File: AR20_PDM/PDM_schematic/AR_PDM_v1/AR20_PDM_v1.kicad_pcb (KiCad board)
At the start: 2 copper layers, 118 x 112 mm, 253 parts, among them IC1 TMUX1208PWR, J1 S_T_?, J2 1-776163-1, K1 DIPxx-1Cxx-51x, K2 DIPxx-1Cxx-51x, P1 B4B-PH-SM4-TB, Q1 BTS50025-1TAD, Q2 BTS50025-1TAD, Q3 BTS50025-1TAD, Q5 BTS50025-1TAD, Q6 BTS50025-1TAD, Q7 BTS50025-1TAD, Q8 BTS50025-1TAD, SW1 SW_DIP_x07, U1 ACM_2020, U10 N-MOS, U11 N-MOS, U12 P-MOS, U13 N-MOS, U14 N-MOS, U15 NMOS, U16 NMOS, U17 NMOS, U18 NMOS, U19 NMOS, U2 INA233, U20 NMOS, U21 NMOS, U22 NMOS, U23 NMOS, U24 NMOS, U25 NMOS, U26 NMOS, U27 NMOS, U28 NMOS, U29 INA233, U3 INA233, U30 INA233, U31 INA233, U32 Fet-P, U33 Fet-P, U34 Fet-P, U35 Fet-P, U36 Fet-P, U4 INA233, U5 INA233, U6 INA233, U7 INA233, U8 INA233, U9 TCA6424ARGJR

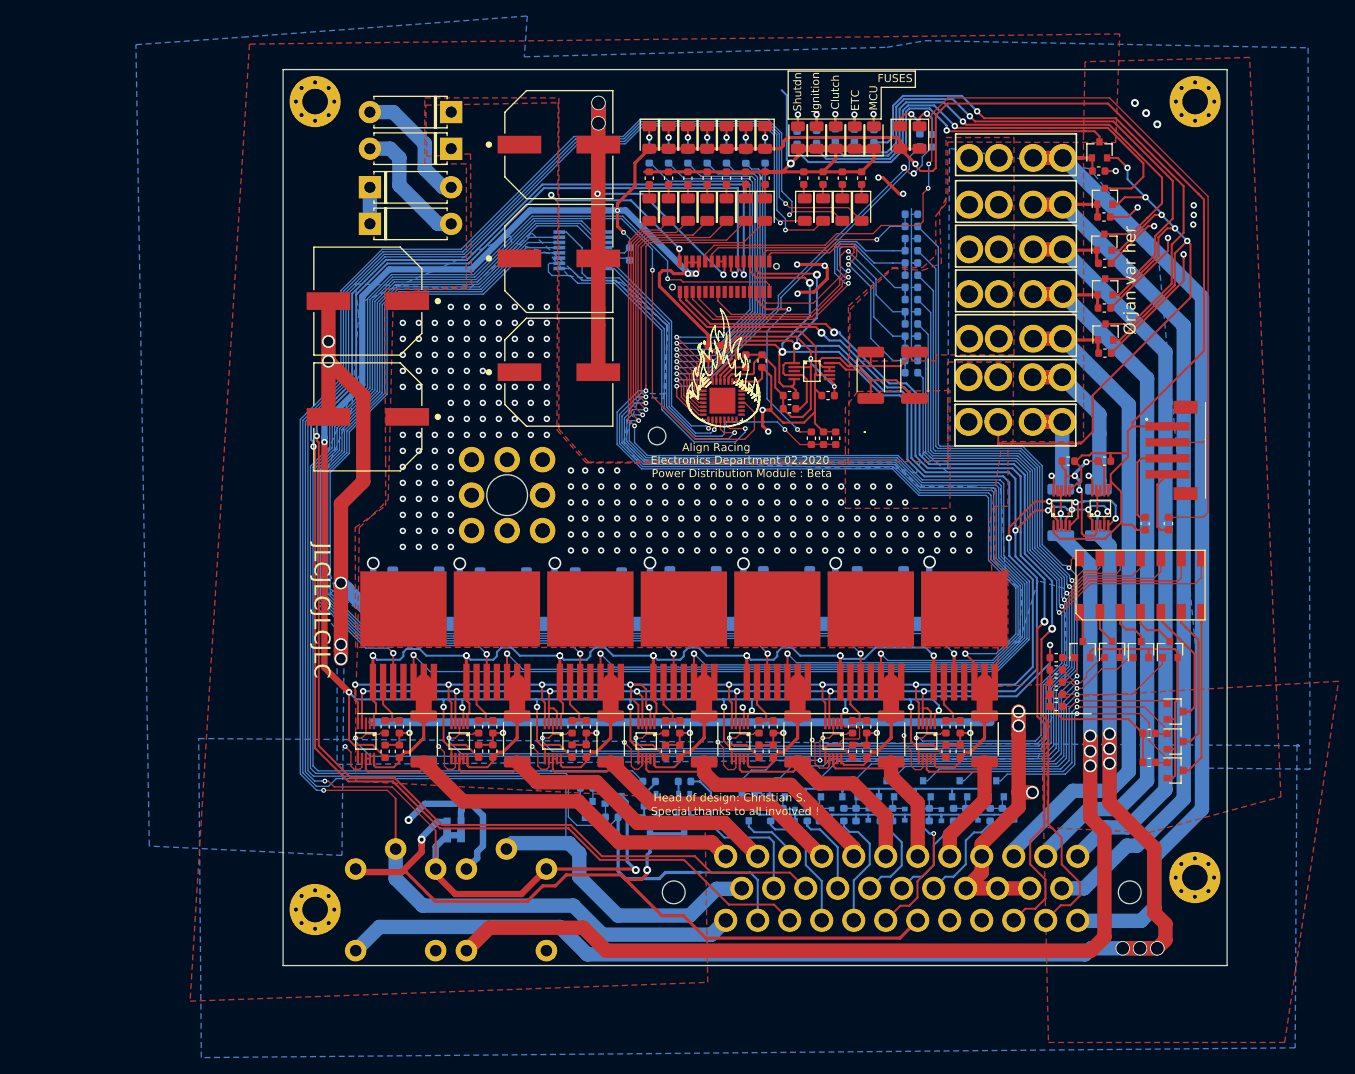
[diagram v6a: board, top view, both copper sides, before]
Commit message: End of Beta beginning of Charlie.
- RE0.2mm rework, jlc pcb minimum clearance with 2 OZ copper, was not advertised, properly
a retrace
Re positioning of some of components
added temp sensor
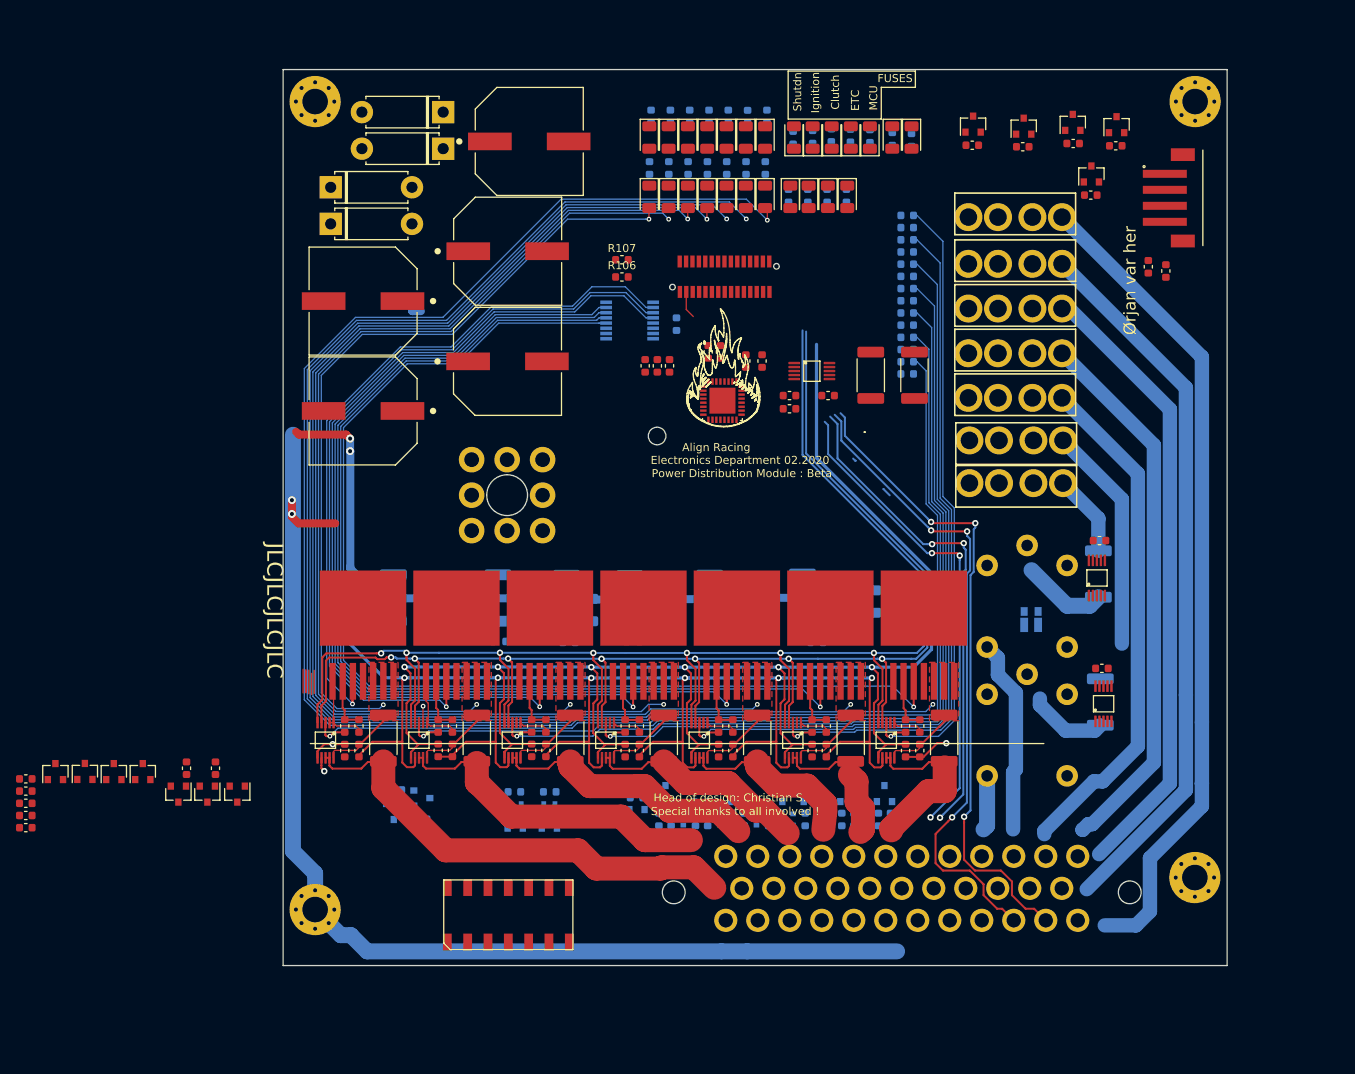
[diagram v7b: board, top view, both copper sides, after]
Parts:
- added R106: NTC, Resistor_SMD:R_0603_1608Metric, F.Cu at (76.2, 62.3)
- added R107: 1k, Resistor_SMD:R_0603_1608Metric, F.Cu at (76.2, 60.1)
- R45, R47, R51, R53, R55, R59, R61, R64, R67, R68, R71: moved to B.Cu
- moved R48 129.7 mm to (1.69, 125.0)
- moved R49 129.7 mm to (1.69, 126.5)
- moved R56 129.7 mm to (1.69, 128.1)
- moved R57 129.7 mm to (1.69, 129.6)
- moved R62 129.7 mm to (1.69, 131.1)
- moved U22 129.3 mm to (5.39, 124.1)
- moved U24 129.3 mm to (12.7, 124.1)
- moved U25 129.3 mm to (16.3, 124.1)
- moved U23 129.3 mm to (9.08, 124.1)
- moved U28 124.6 mm to (20.8, 126.9), turned to 270 degrees
- moved U27 121.1 mm to (24.4, 126.9), turned to 270 degrees
- moved R65 120.3 mm to (21.8, 123.7), turned to 90 degrees
- moved U26 117.7 mm to (28.1, 126.9), turned to 270 degrees
- moved R63 116.8 mm to (25.4, 123.7), turned to 90 degrees
- moved SW1 89.1 mm to (62.0, 142.0)
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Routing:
- net GND: track 961.9 -> 462.3 mm, vias 64 -> 12
- net vcc_5v: track 581.3 -> 213.0 mm, vias 19 -> 8
- net COIL_INJECTOR_OUT: track 224.7 -> 0.00 mm, vias 1 -> 0
- net SHUTDOWN_IN: track 217.8 -> 0.00 mm, vias 1 -> 0
- net FUEL_PUMP_OUT: track 213.4 -> 0.00 mm, vias 2 -> 0
- net Shutdown_Relay_Side: track 212.4 -> 0.00 mm, vias 3 -> 0
- net FP_ENABLE_ACM: track 182.6 -> 0.00 mm, vias 1 -> 0
- net ACM_Shutdown_Circuit: track 158.6 -> 0.00 mm, vias 1 -> 0
- net Net-(K2-Pad14): track 173.3 -> 16.8 mm, vias 7 -> 0
- net V+12V: track 148.4 -> 0.00 mm, vias 244 -> 0
- net RX: track 195.1 -> 60.2 mm, vias 2 -> 3
- net Switch: track 134.4 -> 0.00 mm, vias 2 -> 0
- net TX: track 192.8 -> 61.9 mm, vias 2 -> 3
- net Net-(K1-Pad14): track 146.6 -> 35.1 mm, vias 4 -> 0
- net FP_ENABLE_RELAY_SINK: track 99.8 -> 0.00 mm, vias 2 -> 0
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- added copper zone on F.Cu, net P1_Shunt
- added copper zone on F.Cu, net P2_Shunt
- added copper zone on F.Cu, net P3_Shunt
- added copper zone on F.Cu, net P4_Shunt
- added copper zone on F.Cu, net P5_Shunt
- added copper zone on F.Cu, net P6_Shunt
- added copper zone on F.Cu, net P7_Shunt
- removed copper zone on B.Cu, net GND
- removed copper zone on F.Cu, net GND
- removed copper zone on F.Cu, net Net-(F1-Pad2)
- removed copper zone on B.Cu, net V+12V
- removed copper zone on F.Cu, net V+12V
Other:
- net class Can buss added: clearance 0.2, trace_width 0.25, via_dia 0.8, via_drill 0.4
- net class Default: clearance 0.127 -> 0.2; trace_width 0.25 -> 0.127
- rule trace_clearance: 0.127 -> 0.2

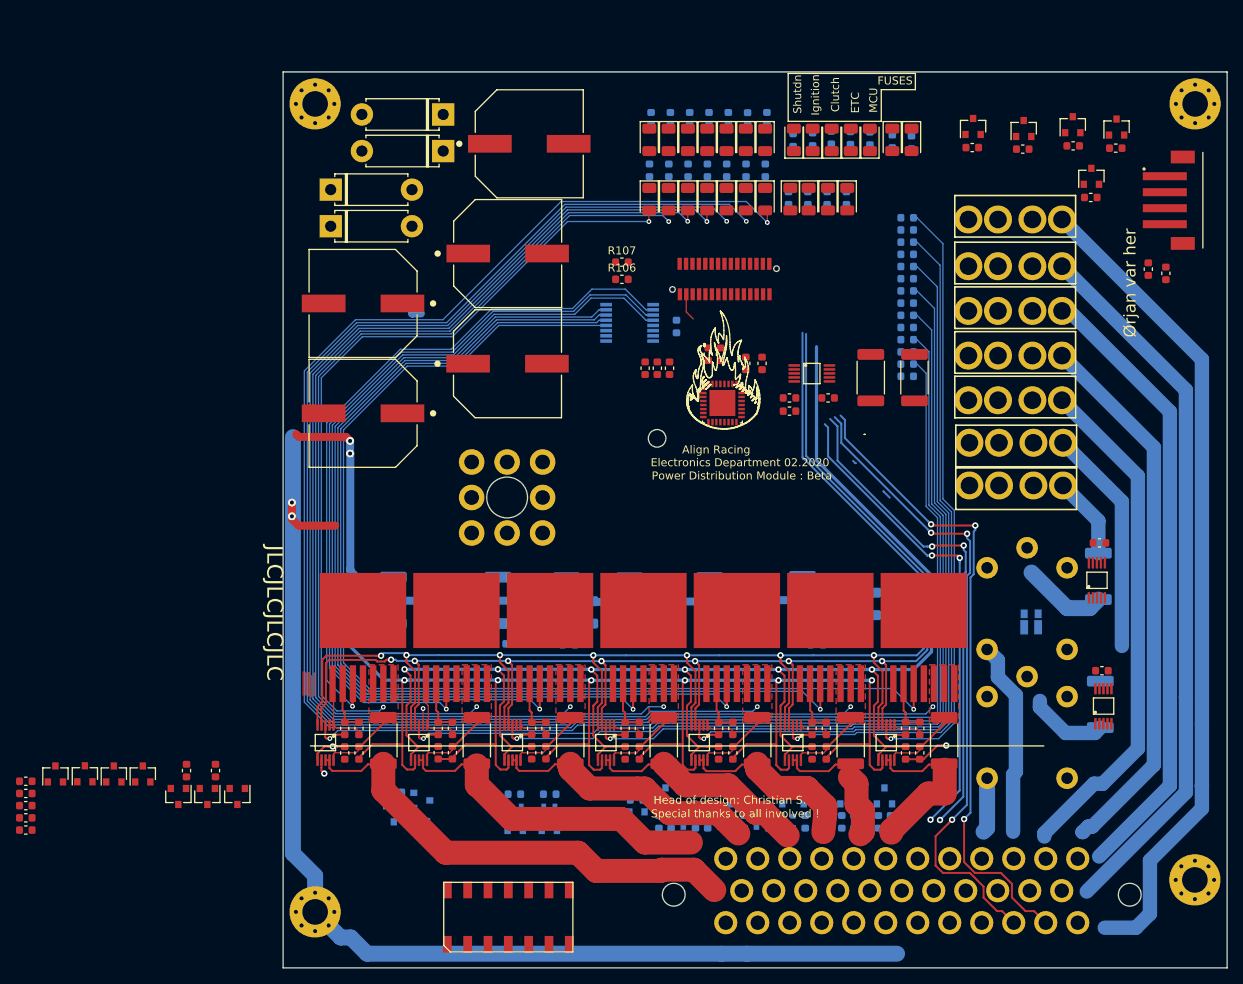
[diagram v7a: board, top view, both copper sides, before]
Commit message: Further testing, reveals pdm needs rework
-  As of now, there are major errors in schematics.
- Needs rework. Version charlie postponed.
- Very nice pcb layout thats almost finished. 
   worth noting this layout for the future
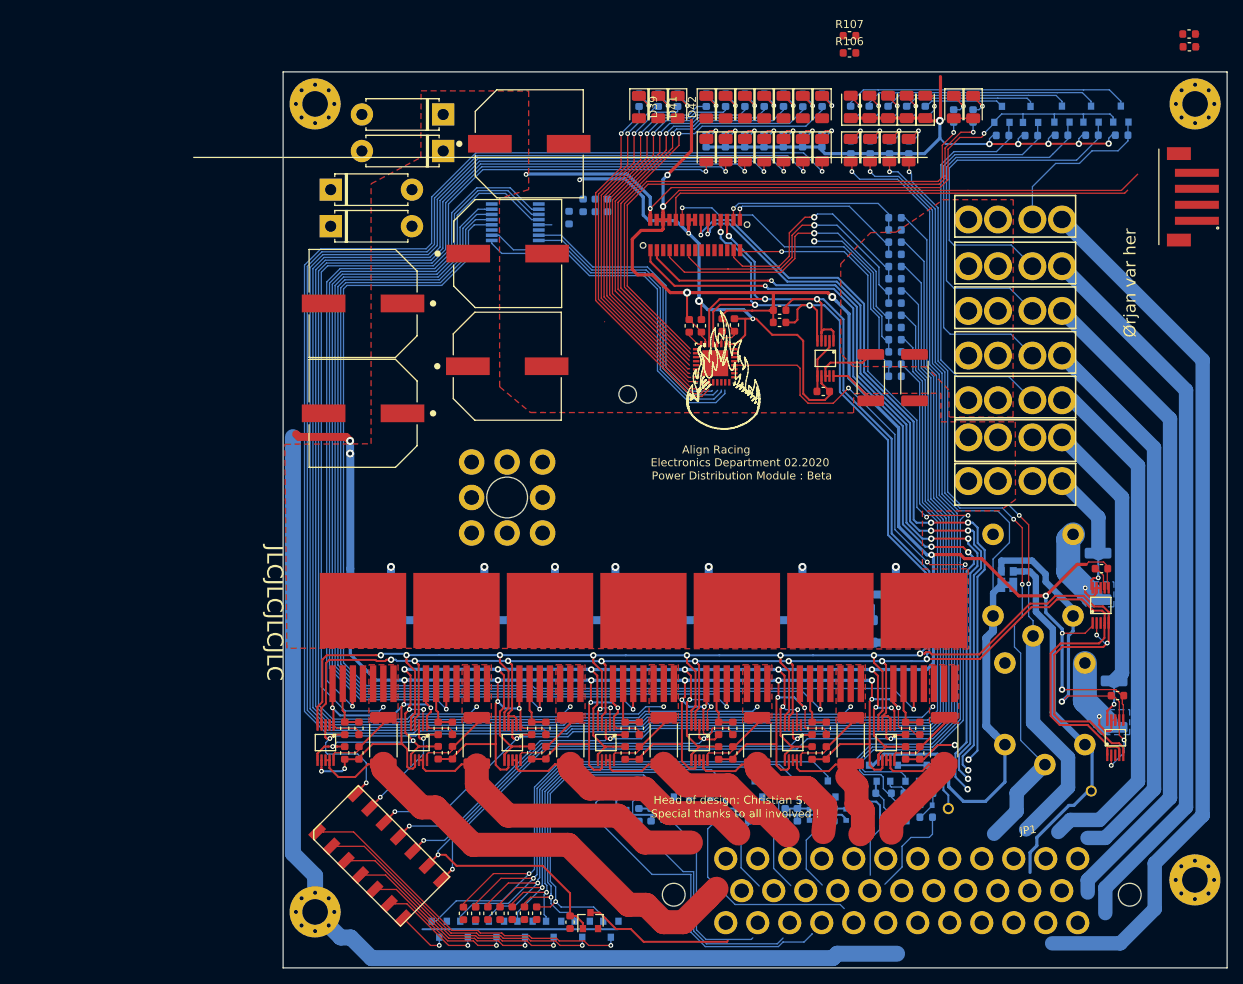
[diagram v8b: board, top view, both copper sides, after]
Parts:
- added D41: P7_Active, LED_SMD:LED_1206_3216Metric, F.Cu at (80.8, 40.7)
- added D42: P7_Active, LED_SMD:LED_1206_3216Metric, F.Cu at (83.2, 40.7)
- added JP1: WireJumper, AR_PDM_v1:WireJumper_12mm, F.Cu at (134.9, 126.2)
- added R108: 153R, Resistor_SMD:R_0603_1608Metric, B.Cu at (83.2, 39.9)
- C6, R1, R100, R102, R2, R76, R96, R98, U22, U23, U24, U25, U26, U27, U28, U32, U33, U34, U35, U36: moved to B.Cu
- D39: value 15V -> P7_Active; footprint AR_PDM_v1:Diode-BZX585-C15,115 -> LED_SMD:LED_1206_3216Metric; moved to F.Cu
- R104: value 4k7 -> 153R
- R17, U10: moved to F.Cu
- R90: value 4K7 -> 153R
- moved R90 91.1 mm to (78.3, 39.9), turned to 270 degrees
- moved D39 88.8 mm to (78.3, 40.7), turned to 270 degrees
- moved R104 88.6 mm to (80.8, 39.9), turned to 270 degrees
- moved U22 72.1 mm to (74.8, 143.5), turned to 270 degrees
- moved R48 66.0 mm to (65.5, 141.5), turned to 270 degrees
- moved U23 65.1 mm to (71.2, 143.5), turned to 270 degrees
- moved R49 64.1 mm to (64.0, 141.5), turned to 270 degrees
- moved U11 63.0 mm to (110.7, 129.1), turned to 180 degrees
- moved R89 62.8 mm to (110.7, 126.5)
- moved R56 62.3 mm to (62.5, 141.5), turned to 270 degrees
- moved R57 60.5 mm to (61.0, 141.5), turned to 270 degrees
- moved R62 58.7 mm to (59.5, 141.5), turned to 270 degrees
- moved U24 58.3 mm to (67.7, 143.5), turned to 270 degrees
- moved R5 56.2 mm to (107.2, 126.5), turned to 180 degrees
- moved U12 56.0 mm to (107.1, 124.0), turned to 90 degrees
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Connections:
- D31 pad 2: FP_ENABLE_RELAY_SINK -> Net-(D31-Pad2)
- D39 pad 2: GND -> vcc_5v
- K2 pad 2: FP_ENABLE_RELAY_SINK -> Net-(D31-Pad2)
- R104 pad 1: Net-(D39-Pad1) -> Net-(D41-Pad1)
- R104 pad 2: FP_ENABLE_ACM -> Status_2
- R90 pad 2: GND -> Status_1
- U13 pad 1: Net-(D39-Pad1) -> FP_ENABLE_ACM
- U9 pad 14: Net-(U9-Pad14) -> Status_1
- U9 pad 15: Net-(U9-Pad15) -> Status_2
- U9 pad 16: Net-(U9-Pad16) -> Status_3
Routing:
- net GND: track 462.3 -> 817.8 mm, vias 12 -> 37
- net vcc_5v: track 213.0 -> 448.1 mm, vias 8 -> 24
- net V+12V: track 0.00 -> 142.2 mm, vias 0 -> 10
- net Shutdown_Relay_Side: track 0.00 -> 118.0 mm, vias 0 -> 1
- net SDA: track 180.3 -> 290.3 mm, vias 7 -> 11
- net SHUTDOWN_IN: track 0.00 -> 109.5 mm, vias 0 -> 1
- net SLC: track 186.5 -> 294.3 mm, vias 7 -> 15
- net ACM_Shutdown_Circuit: track 0.00 -> 106.8 mm, vias 0 -> 3
- net FUEL_PUMP_OUT: track 0.00 -> 99.2 mm, vias 0 -> 3
- net COIL_INJECTOR_OUT: track 0.00 -> 97.4 mm, vias 0 -> 3
- net FP_ENABLE_ACM: track 0.00 -> 91.4 mm, vias 0 -> 3
- net P6_MOS_IN: track 86.5 -> 163.9 mm, vias 1 -> 2
- net Net-(R65-Pad1): track 0.00 -> 75.3 mm, vias 0 -> 1
- net COIL_INJECTOR_Fault: track 0.00 -> 71.8 mm, vias 0 -> 1
- net FUEL_PUMP_Fault: track 0.00 -> 70.6 mm, vias 0 -> 1
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- added copper zone on F.Cu, net Net-(F1-Pad2)
- added copper zone on B.Cu, net Net-(K1-Pad14)
- added copper zone on B.Cu, net Net-(K2-Pad14)
- added copper zone on F.Cu, net V+12V
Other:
- board text removed: "Clutch"
- board text removed: "ETC"
- board text removed: "FUSES"
- board text removed: "Ignition"
- board text removed: "MCU"
- board text removed: "Shutdn"
